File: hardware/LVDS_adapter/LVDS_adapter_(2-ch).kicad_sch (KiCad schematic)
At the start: 8 parts, among them J1 DF12NB(3.0)-30DS-0.5V(51), J2 LVDS, J3 BL_POWER, J4 DF12NB(3.0)-30DS-0.5V(51)

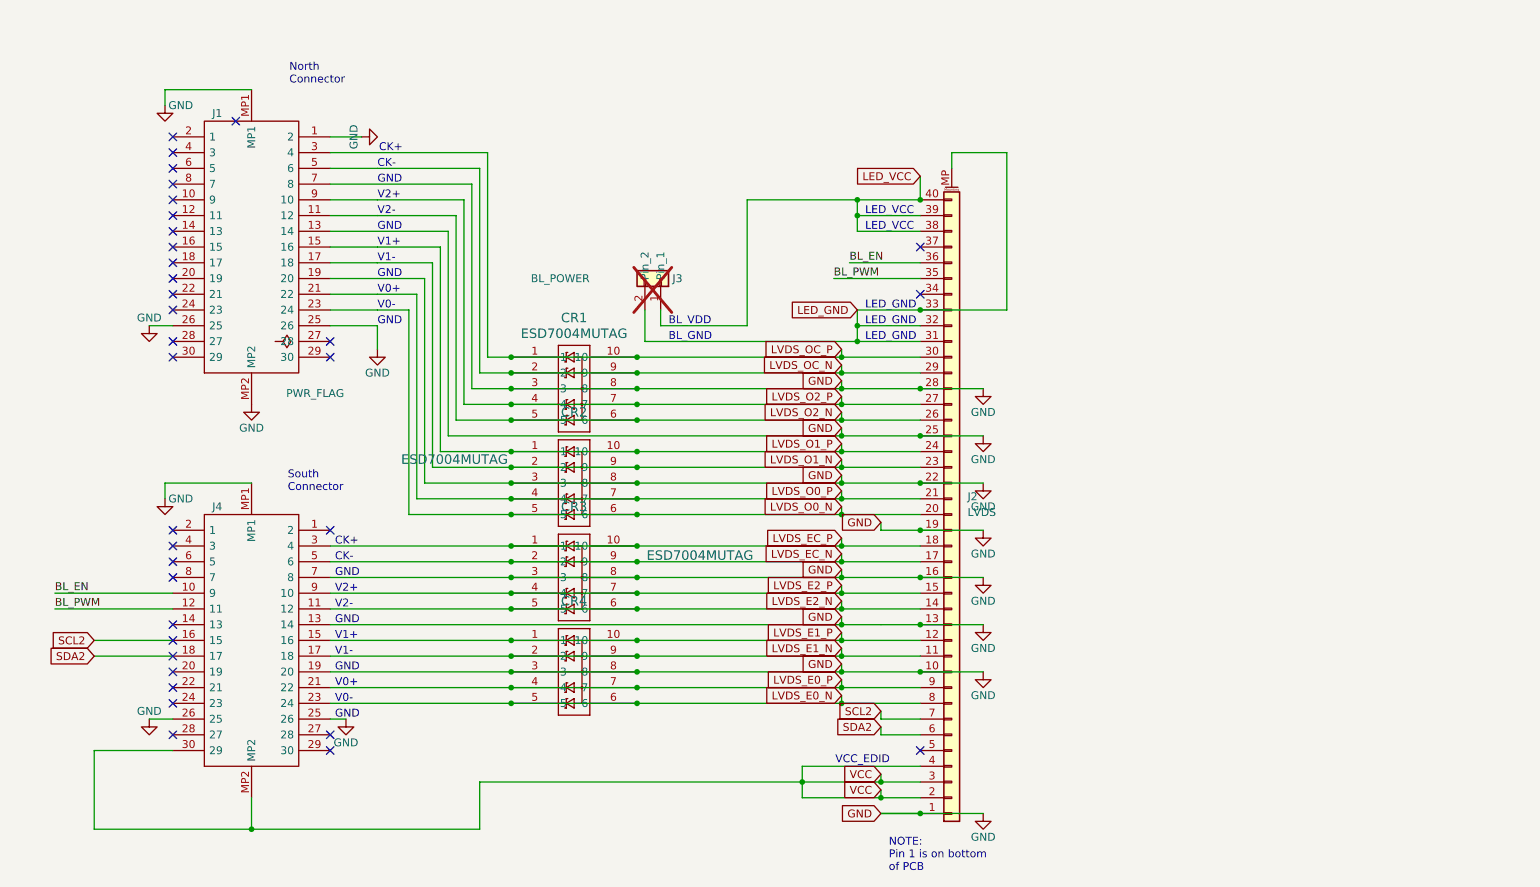
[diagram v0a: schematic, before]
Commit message: make 4 layers for better signal integrity and add DC-DC for backlight
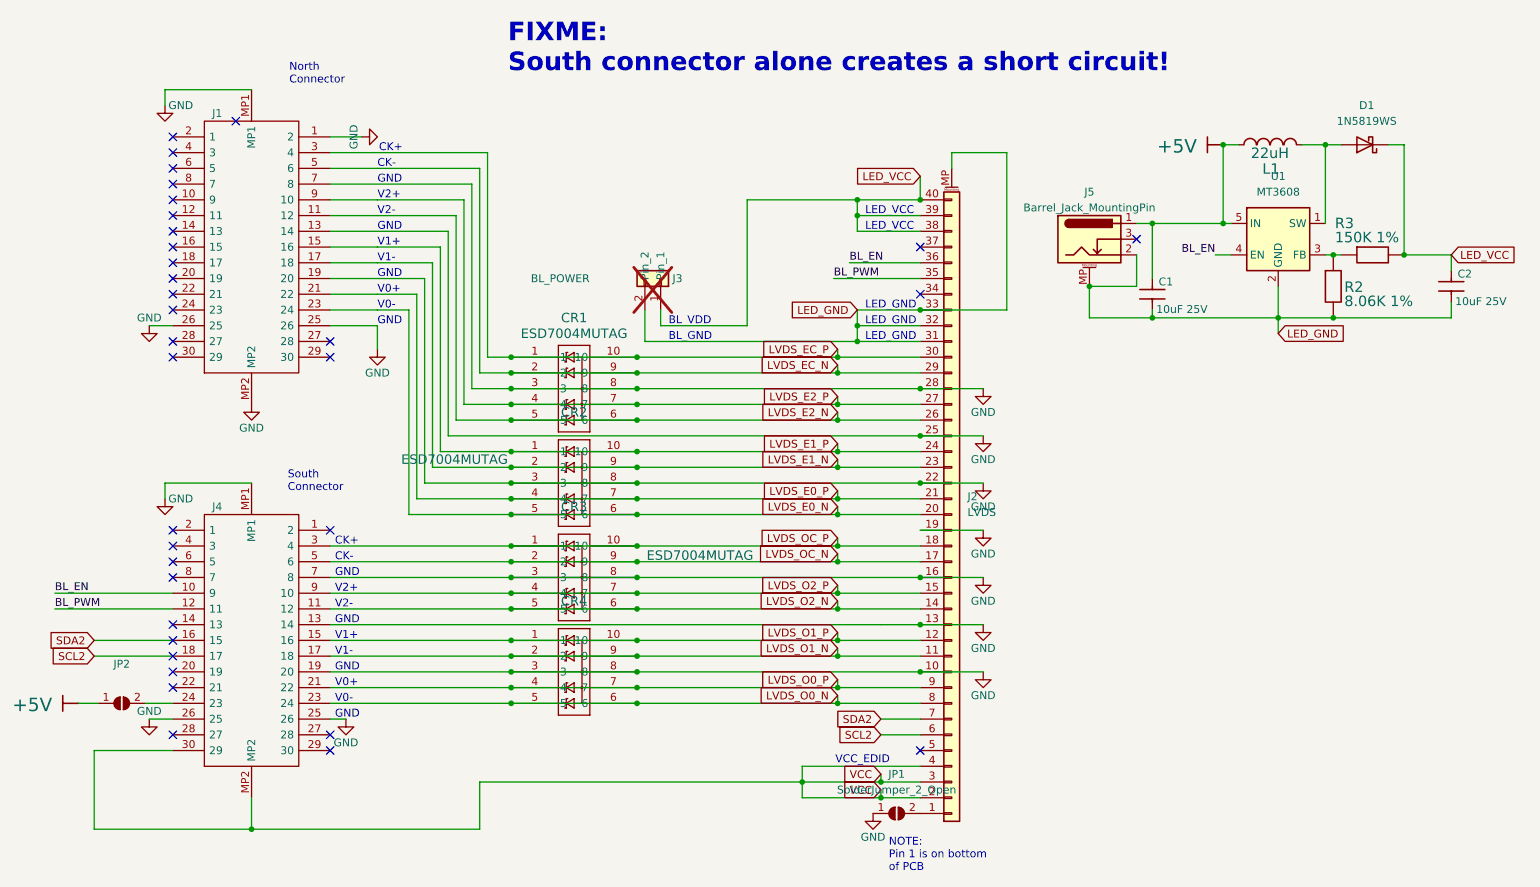
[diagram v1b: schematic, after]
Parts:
- added C1, C2: 10uF 25V, Capacitor_SMD:C_0805_2012Metric, symbol Periph-altium-import:0_CAP
- added D1: 1N5819WS, Diode_SMD:D_SOD-323, symbol Diode:1N5819WS
- added J5: Barrel_Jack_MountingPin, easyeda2kicad:DC-IN-SMD_DC-045A-13A, symbol Connector:Barrel_Jack_Switch_MountingPin
- added JP1: SolderJumper_2_Open, Jumper:SolderJumper-2_P1.3mm_Open_RoundedPad1.0x1.5mm, symbol Jumper:SolderJumper_2_Open
- added JP2: SolderJumper_2_Open, symbol Jumper:SolderJumper_2_Open
- added L1: 22uH, Inductor_SMD:L_Cenker_CKCS4020, symbol CKCS201610-2.2UH/M-N_1
- added R2: 8.06K 1%, Resistor_SMD:R_0402_1005Metric, symbol R_0402_EU_1
- added R3: 150K 1%, Resistor_SMD:R_0402_1005Metric, symbol R_0402_EU
- added U1: MT3608, Package_TO_SOT_SMD:SOT-23-6, symbol Regulator_Switching:MT3608
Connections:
- net BL_EN: now also U1.4 (EN)
- net GND: now also JP1.1 (A); no longer J2.1 (Pin_1)
- net LED_GND: now also C1.2, C2.2, J5.2, J5.MP (MountPin), R2.2, U1.2 (GND)
- net LED_VCC: now also C2.1, D1.1 (K), R3.2
- net LVDS_E0_N: now also CR2.5, CR2.6, J1.23 (24), J2.20 (Pin_20); no longer CR4.5, CR4.6, J2.8 (Pin_8), J4.23 (24)
- net LVDS_E0_P: now also CR2.4, CR2.7, J1.21 (22), J2.21 (Pin_21); no longer CR4.4, CR4.7, J2.9 (Pin_9), J4.21 (22)
- net LVDS_E1_N: now also CR2.2, CR2.9, J1.17 (18), J2.23 (Pin_23); no longer CR4.2, CR4.9, J2.11 (Pin_11), J4.17 (18)
- net LVDS_E1_P: now also CR2.1, CR2.10, J1.15 (16), J2.24 (Pin_24); no longer CR4.1, CR4.10, J2.12 (Pin_12), J4.15 (16)
- net LVDS_E2_N: now also CR1.5, CR1.6, J1.11 (12), J2.26 (Pin_26); no longer CR3.5, CR3.6, J2.14 (Pin_14), J4.11 (12)
- net LVDS_E2_P: now also CR1.4, CR1.7, J1.9 (10), J2.27 (Pin_27); no longer CR3.4, CR3.7, J2.15 (Pin_15), J4.9 (10)
- net LVDS_EC_N: now also CR1.2, CR1.9, J1.5 (6), J2.29 (Pin_29); no longer CR3.2, CR3.9, J2.17 (Pin_17), J4.5 (6)
- net LVDS_EC_P: now also CR1.1, CR1.10, J1.3 (4), J2.30 (Pin_30); no longer CR3.1, CR3.10, J2.18 (Pin_18), J4.3 (4)
- net LVDS_O0_N: now also CR4.5, CR4.6, J2.8 (Pin_8), J4.23 (24); no longer CR2.5, CR2.6, J1.23 (24), J2.20 (Pin_20)
- net LVDS_O0_P: now also CR4.4, CR4.7, J2.9 (Pin_9), J4.21 (22); no longer CR2.4, CR2.7, J1.21 (22), J2.21 (Pin_21)
- net LVDS_O1_N: now also CR4.2, CR4.9, J2.11 (Pin_11), J4.17 (18); no longer CR2.2, CR2.9, J1.17 (18), J2.23 (Pin_23)
- net LVDS_O1_P: now also CR4.1, CR4.10, J2.12 (Pin_12), J4.15 (16); no longer CR2.1, CR2.10, J1.15 (16), J2.24 (Pin_24)
- net LVDS_O2_N: now also CR3.5, CR3.6, J2.14 (Pin_14), J4.11 (12); no longer CR1.5, CR1.6, J1.11 (12), J2.26 (Pin_26)
- net LVDS_O2_P: now also CR3.4, CR3.7, J2.15 (Pin_15), J4.9 (10); no longer CR1.4, CR1.7, J1.9 (10), J2.27 (Pin_27)
- net LVDS_OC_N: now also CR3.2, CR3.9, J2.17 (Pin_17), J4.5 (6); no longer CR1.2, CR1.9, J1.5 (6), J2.29 (Pin_29)
- net LVDS_OC_P: now also CR3.1, CR3.10, J2.18 (Pin_18), J4.3 (4); no longer CR1.1, CR1.10, J1.3 (4), J2.30 (Pin_30)
- net SCL2: now also J2.6 (Pin_6), J4.18 (17); no longer J2.7 (Pin_7), J4.16 (15)
- net SDA2: now also J2.7 (Pin_7), J4.16 (15); no longer J2.6 (Pin_6), J4.18 (17)
- net at J4.24 (23): now also JP2.2 (B)
- new net: J2.1 (Pin_1), JP1.2 (B)
- new net: R2.1, R3.1, U1.3 (FB)
- new net: D1.2 (A), L1.2, U1.1 (SW)
- new net +5V: C1.1, J5.1, JP2.1 (A), L1.1, U1.5 (IN)
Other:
- note added: "FIXME: South connector alone creates a short circuit!"
